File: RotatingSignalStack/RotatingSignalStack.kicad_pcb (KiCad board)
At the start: 2 copper layers, 92 parts, among them IC2 STM32H562RIT6, J2 Conn_01x04, J3 RJ45_LED_Shielded, SW1 SW_Push, SW2 Boot Switch, SW5 SW_Push, SW6 SW_Push, SW7 SW_Push, T1 GMG116S1202R, U1 TMAG5273C1QDBVR, U2 AP63203WU-7, U3 SN65HVD232, U4 DP83825I, U5 SG-210STF 50.0000ML0, U6 USBLC6-2SC6, U7 USBLC6-4SC6

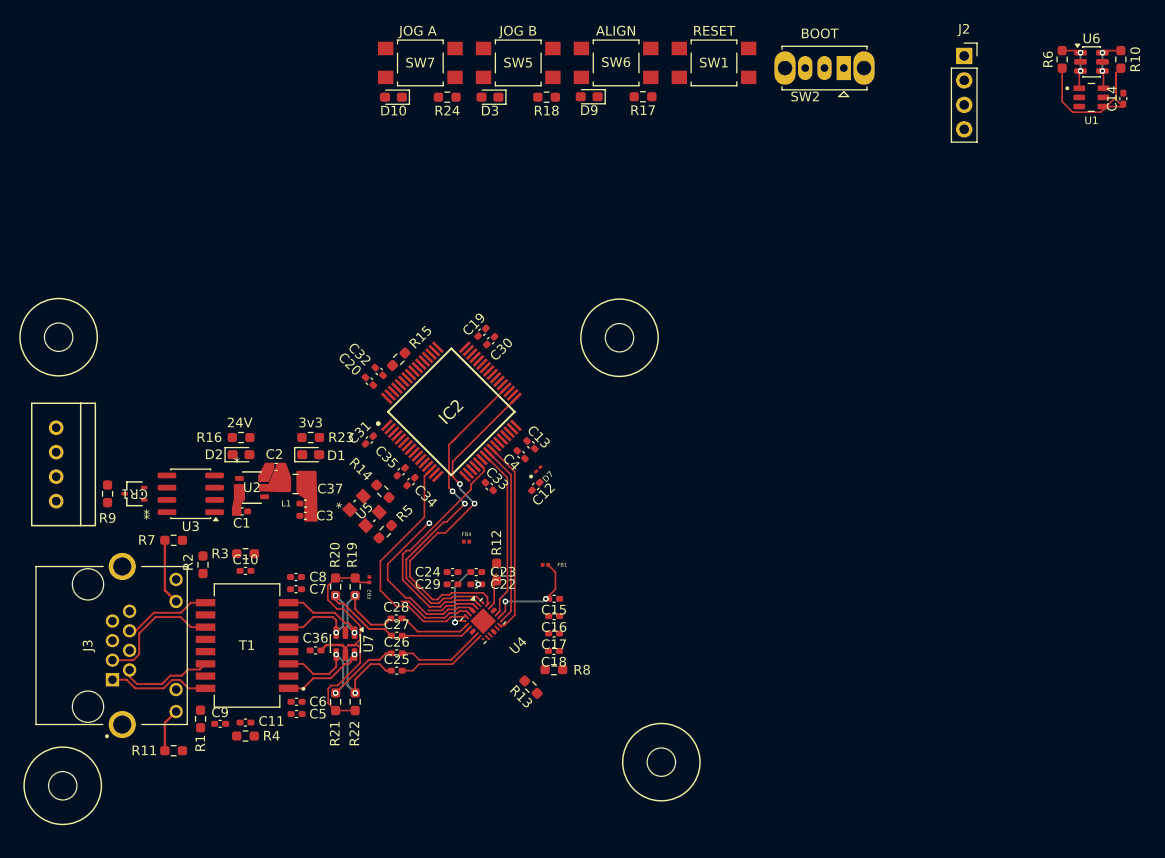
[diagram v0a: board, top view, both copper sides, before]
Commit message: Finished traces, added silkscreen
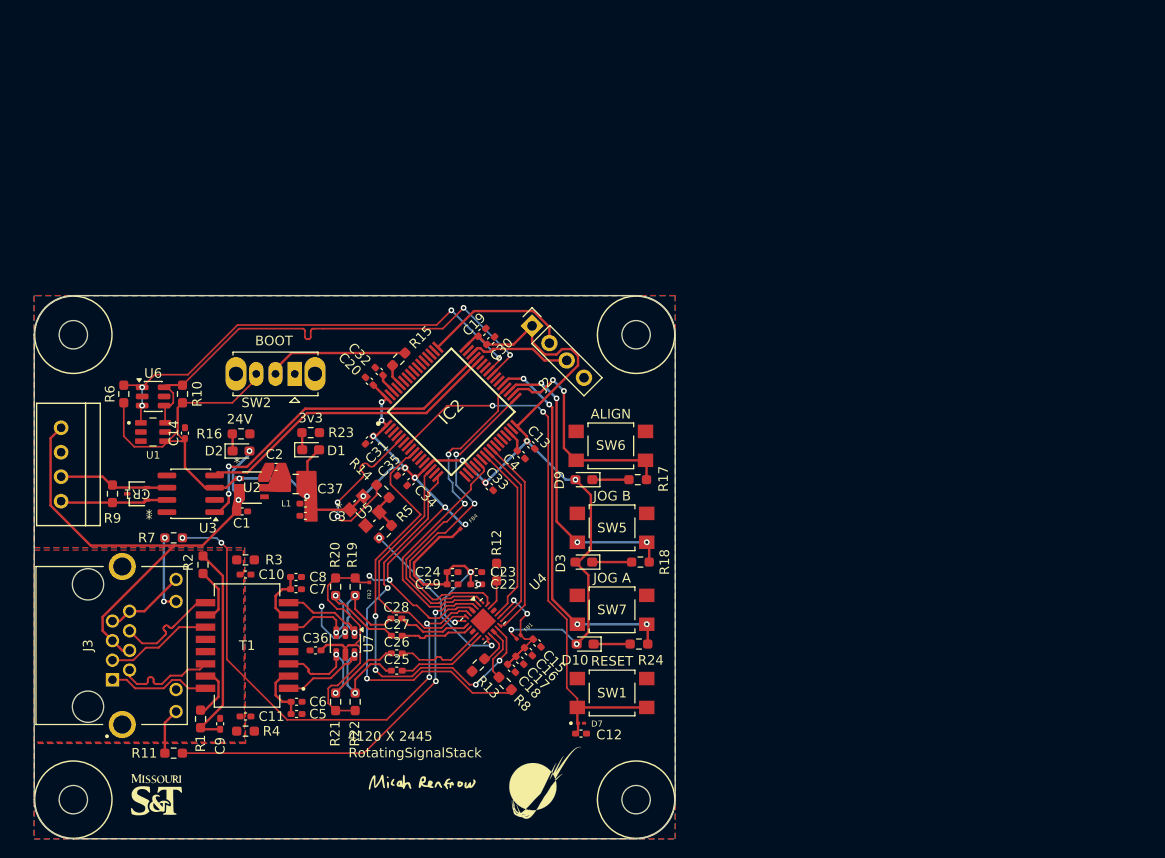
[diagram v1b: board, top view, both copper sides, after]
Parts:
- added G***: LOGO, Silkscreens:MST, F.Cu at (136.9, 107.4)
- added G***: LOGO, LOGO, F.Cu at (164.5, 106.2)
- added G***: LOGO, MRDT_Silkscreens:0_MRDT_Logo_7.5mm, F.Cu at (177.3, 106.2)
- moved C14 103.4 mm to (139.9, 69.9)
- moved R6 103.4 mm to (133.5, 65.8)
- moved U1 103.4 mm to (136.5, 69.8)
- moved R10 103.4 mm to (139.6, 65.8)
- moved U6 103.4 mm to (136.6, 66.1)
- moved SW1 66.3 mm to (184.2, 96.9)
- moved SW2 65.2 mm to (151.3, 63.8)
- moved D10 60.2 mm to (181.4, 91.8)
- moved R24 60.2 mm to (187.0, 91.8)
- moved SW7 60.2 mm to (184.2, 88.2)
- moved J2 52.9 mm to (175.9, 58.8), turned to 45 degrees
- moved D3 49.2 mm to (181.3, 83.3)
- moved R18 49.2 mm to (187.1, 83.3)
- moved SW5 49.2 mm to (184.2, 79.7)
- moved D9 39.8 mm to (181.3, 74.7)
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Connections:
- net Net-(U4-RD+) renamed /PHY/RD+
- net Net-(U4-RD-) renamed /PHY/RD-
- net Net-(U4-TD+) renamed /PHY/TD+
- net Net-(U4-TD-) renamed /PHY/TD-
- IC2 pad 3: /Buttons/JOG B -> unconnected-(IC2-PC14-OSC32_IN-Pad3)
- IC2 pad 34: unconnected-(IC2-PB13-Pad34) -> /Buttons/ALIGN
- IC2 pad 35: unconnected-(IC2-PB14-Pad35) -> /Buttons/JOG B
- IC2 pad 37: unconnected-(IC2-PC6-Pad37) -> /Buttons/JOG A
- IC2 pad 4: /Buttons/JOG A -> unconnected-(IC2-PC15-OSC32_OUT-Pad4)
- IC2 pad 6: /Buttons/ALIGN -> unconnected-(IC2-PH1-OSC_OUT-Pad6)
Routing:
- net VBAT: track 37.7 -> 187.6 mm, vias 1 -> 18
- net Net-(IC2-NRST): track 0.00 -> 58.3 mm, vias 0 -> 2
- net VBUS: track 0.00 -> 53.9 mm, vias 0 -> 2
- net /Compass/I2C3_SDA: track 5.73 -> 52.7 mm
- net /PHY/MDC: track 0.00 -> 46.4 mm, vias 0 -> 4
- net Net-(U4-LED0/S(ANEG_Dis)): track 8.18 -> 52.8 mm, vias 0 -> 4
- net /Compass/I2C3_SCL: track 6.09 -> 50.0 mm, vias 2 -> 4
- net /PHY/MDIO: track 0.00 -> 40.8 mm, vias 0 -> 2
- net /Buttons/JOG A: track 0.00 -> 39.6 mm, vias 0 -> 4
- net /CAN/DCAN1_TX: track 0.00 -> 35.9 mm, vias 0 -> 2
- net Net-(U4-50MHzOut/LED2/S(RX_DV_EN)): track 5.49 -> 41.3 mm, vias 0 -> 2
- net /CAN/DCAN1_RX: track 0.00 -> 32.3 mm
- net /Buttons/JOG B: track 0.00 -> 31.1 mm, vias 0 -> 4
- net /Buttons/ALIGN: track 0.00 -> 23.7 mm, vias 0 -> 2
- net Net-(C9-Pad1): track 0.00 -> 21.7 mm
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- added copper zone on F.Cu, net GNDPWR
- added copper zone on B.Cu, net VSSA
- added copper zone on F.Cu, net VSSA
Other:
- board outline added: 66.5 x 56.4 mm
- board text added: "4120 X 2445"
- board text added: "RotatingSignalStack"

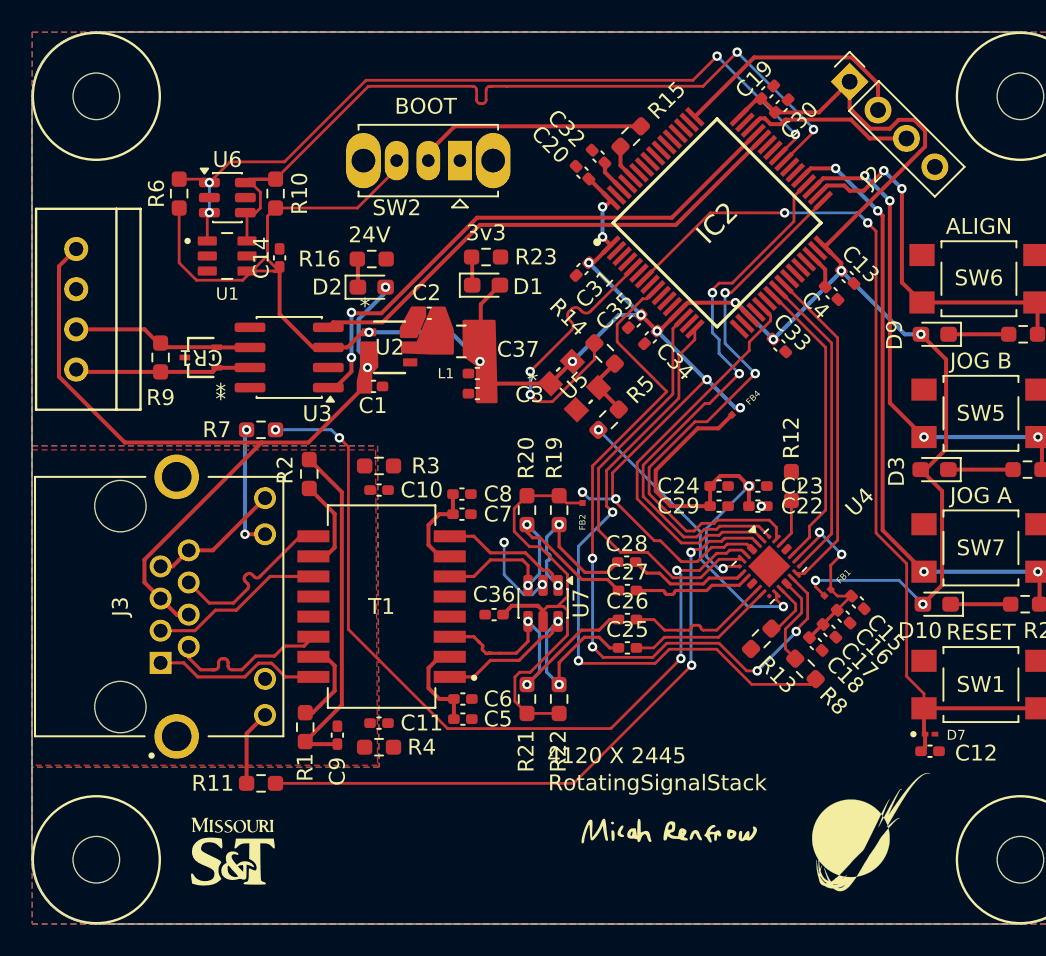
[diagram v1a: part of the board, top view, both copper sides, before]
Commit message: More changes
compass and oki conn and 6 pin conn with the old DIR/EN/STP/COM, fix trace length, under 50 mil Vbus, tree branch
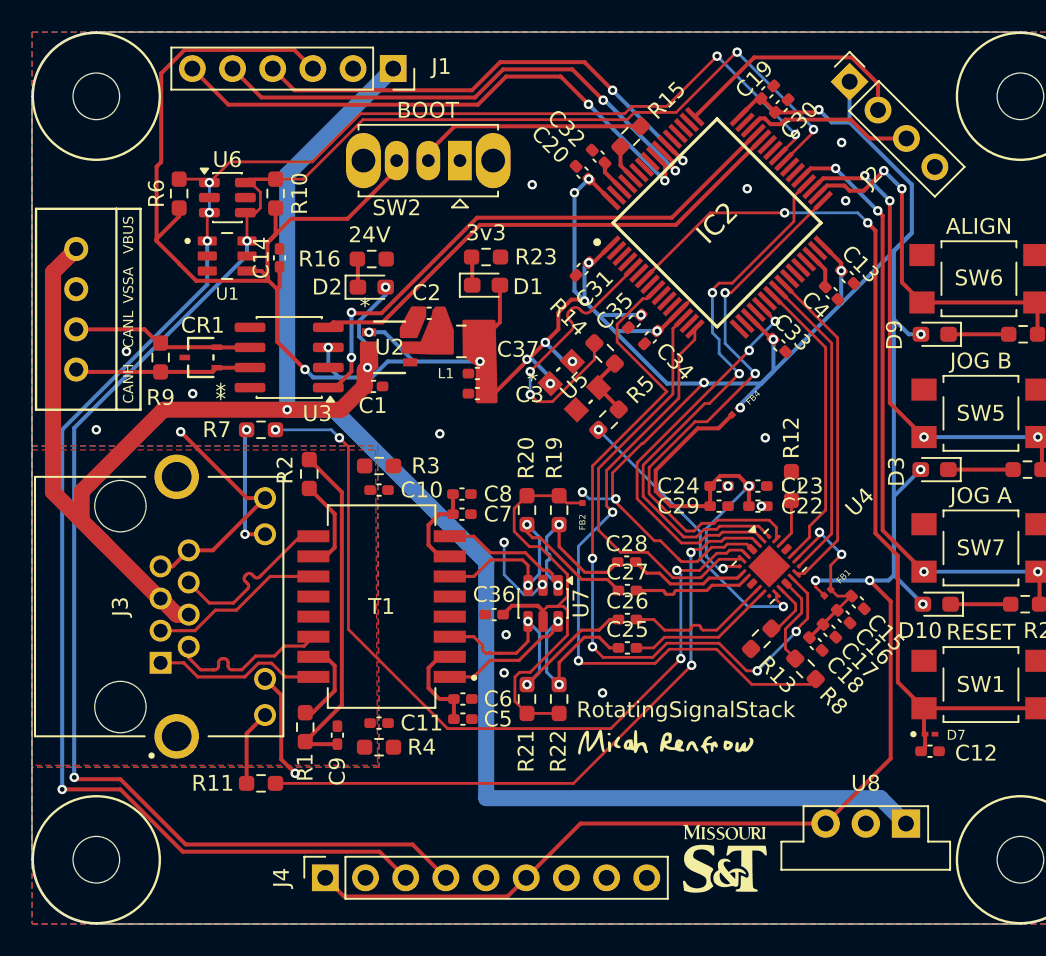
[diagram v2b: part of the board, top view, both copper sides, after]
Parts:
- removed the G*** at (177.3, 106.2)
- added J1: Conn_01x06, Connector_PinSocket_2.54mm:PinSocket_1x06_P2.54mm_Vertical, F.Cu at (147.0, 57.9)
- added J4: Conn_01x09, Connector_PinSocket_2.54mm:PinSocket_1x09_P2.54mm_Vertical, F.Cu at (142.7, 109.1)
- added U8: OKI-78SR-3.3_1.5-W36-C, Converter_DCDC:Converter_DCDC_Murata_OKI-78SR_Vertical, F.Cu at (179.5, 105.7)
- R23: value 1.5k -> 330
- moved G*** 31.1 mm to (168.0, 107.9)
- moved G*** 5.62 mm to (164.2, 100.6)
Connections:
- net /Compass/I2C3_SCL renamed SCL
- net /Compass/I2C3_SDA renamed SDA
- IC2 pad 54: unconnected-(IC2-PD2-Pad54) -> EN
- IC2 pad 55: unconnected-(IC2-PB3-Pad55) -> STP
- IC2 pad 56: unconnected-(IC2-PB4-Pad56) -> DIR
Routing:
- net VBAT: track 187.6 -> 290.4 mm, vias 18 -> 26
- net VBUS: track 53.9 -> 142.8 mm, vias 2 -> 3
- net SDA: track 52.7 -> 115.5 mm, vias 2 -> 4
- net SCL: track 50.0 -> 112.5 mm, vias 4 -> 6
- net DIR: track 0.00 -> 36.1 mm, vias 0 -> 2
- net STP: track 0.00 -> 33.8 mm, vias 0 -> 2
- net EN: track 0.00 -> 31.2 mm, vias 0 -> 2
- net VSSA: track 13.7 -> 27.6 mm, vias 3 -> 18
- net /PHY/TX_EN: track 25.4 -> 26.5 mm, vias 0 -> 2
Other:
- board text added: "CANH"
- board text added: "CANL"
- board text added: "VBUS"
- board text added: "VSSA"
- board text removed: "4120 X 2445"

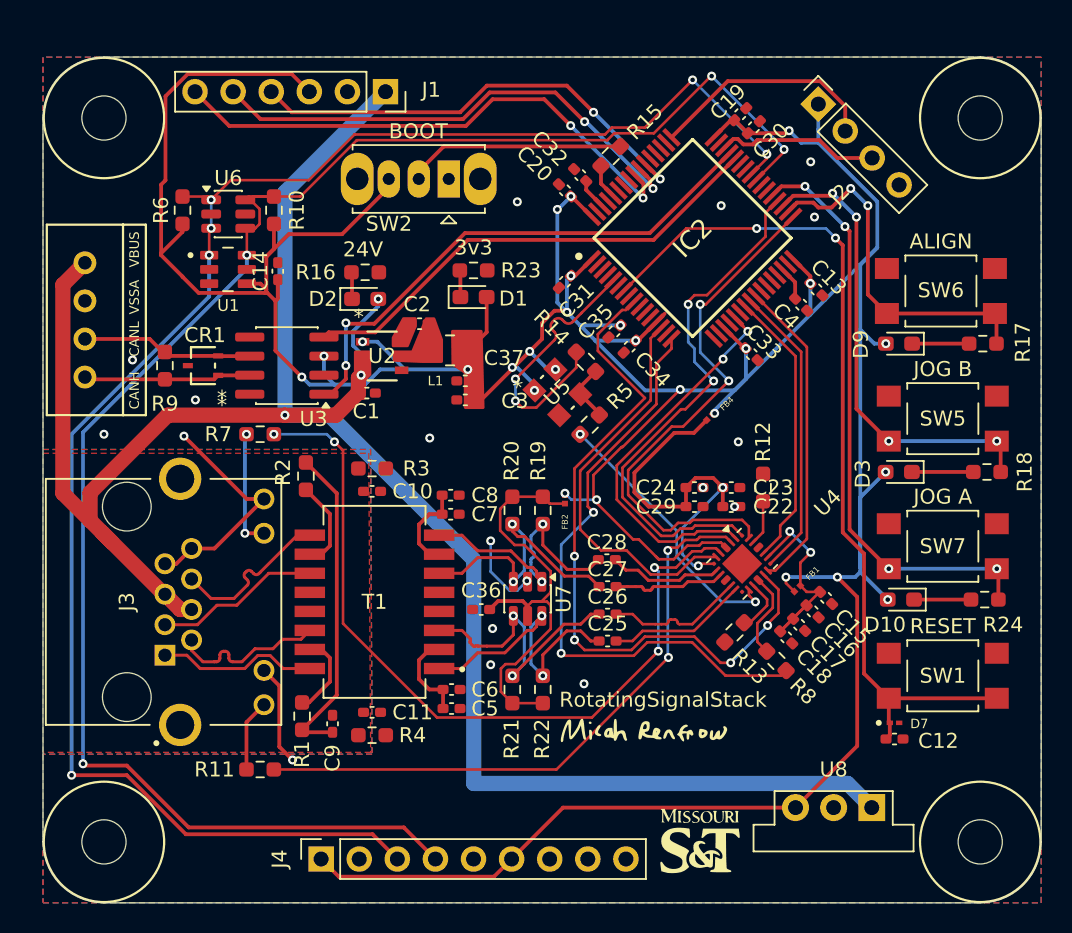
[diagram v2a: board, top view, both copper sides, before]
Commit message: Added ground edges and fixed capacitors and layout issues
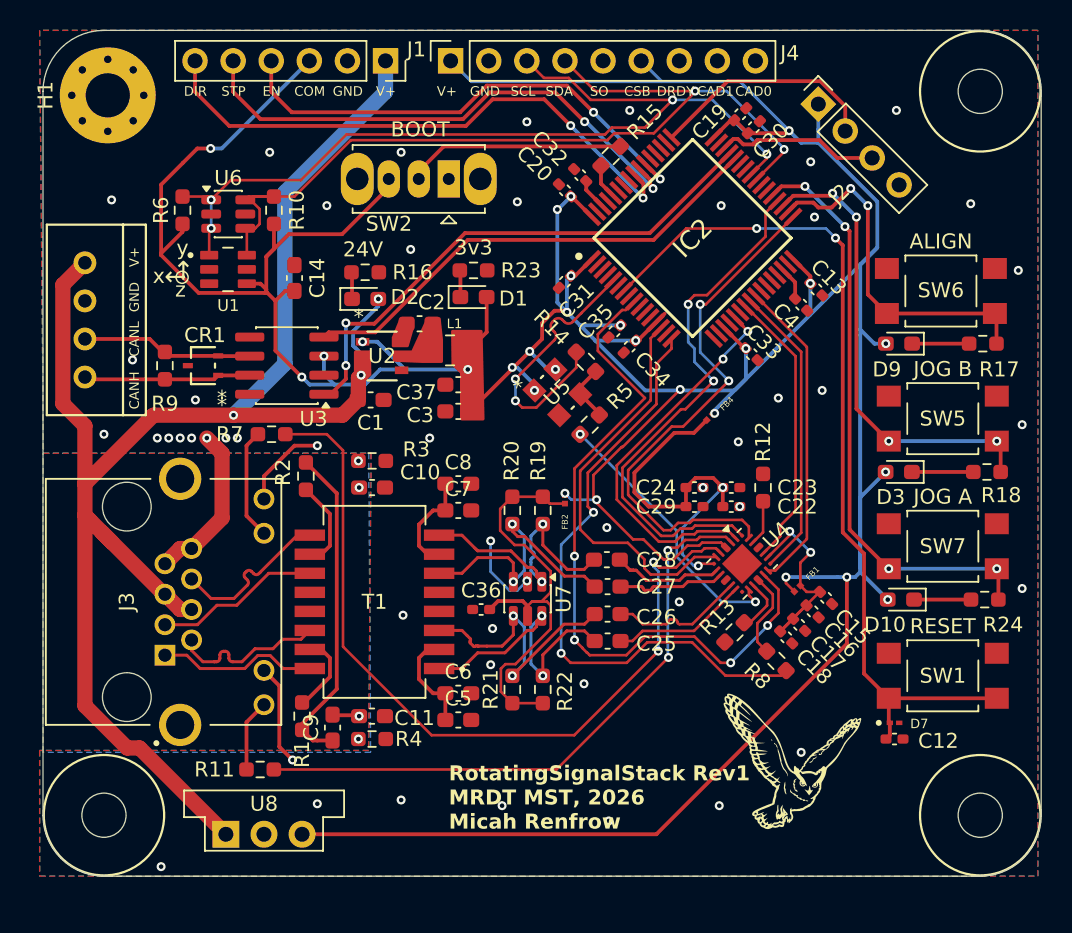
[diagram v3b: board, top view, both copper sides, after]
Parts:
- removed the G*** at (168.0, 107.9)
- C1, C10, C11, C14, C2, C25, C26, C27, C28, C3, C37, C5, C6, C7, C8, C9: footprint Capacitor_SMD:C_0402_1005Metric_Pad0.74x0.62mm_HandSolder -> Capacitor_SMD:C_0603_1608Metric_Pad1.08x0.95mm_HandSolder
- G***: moved to B.Cu
- H1: footprint MRDT_Drill_Holes:4_40_Hole_Corner -> MountingHole:MountingHole_3.2mm_M3_Pad_Via
- moved J4 53.9 mm to (151.4, 55.9)
- moved U8 43.1 mm to (136.4, 107.4), turned to 0 degrees
- moved G*** 19.6 mm to (157.5, 82.2), turned to 180 degrees
- moved H1 6.67 mm to (128.5, 58.2)
- moved J1 2.06 mm to (147.0, 55.9)
- moved H2 1.78 mm to (182.7, 61.9)
- moved H3 1.78 mm to (132.3, 102.2)
- moved H4 1.78 mm to (182.7, 102.2)
- moved C14 1.20 mm to (141.0, 70.4)
- moved C8 0.92 mm to (151.9, 84.1)
- moved C3 0.89 mm to (151.9, 79.2)
- moved C5 0.88 mm to (151.9, 99.8)
- moved R7 0.76 mm to (139.4, 80.8)
- moved C7 0.57 mm to (151.9, 85.9)
- moved C37 0.53 mm to (151.9, 77.5)
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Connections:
- C1 pad 2: VSSA -> GND
- C10 pad 2: VSSA -> GND
- C11 pad 2: VSSA -> GND
- C12 pad 2: VSSA -> GND
- C13 pad 1: VBAT -> +3V3
- C13 pad 2: VSSA -> GND
- C14 pad 1: VBAT -> +3V3
- C14 pad 2: VSSA -> GND
- C15 pad 1: VSSA -> GND
- C16 pad 1: VSSA -> GND
- C17 pad 1: VSSA -> GND
- C18 pad 1: VSSA -> GND
- C19 pad 1: VBAT -> +3V3
- C19 pad 2: VSSA -> GND
- C20 pad 1: VBAT -> +3V3
- C20 pad 2: VSSA -> GND
- C22 pad 2: VSSA -> GND
- C23 pad 2: VSSA -> GND
- C24 pad 2: VSSA -> GND
- C29 pad 2: VSSA -> GND
- C3 pad 1: VBAT -> +3V3
- C3 pad 2: VSSA -> GND
- C30 pad 1: VBAT -> +3V3
- C30 pad 2: VSSA -> GND
- C31 pad 1: VBAT -> +3V3
- C31 pad 2: VSSA -> GND
- C32 pad 1: VSSA -> GND
- C33 pad 1: VBAT -> +3V3
- C33 pad 2: VSSA -> GND
- C34 pad 1: VBAT -> +3V3
- C34 pad 2: VSSA -> GND
- C35 pad 1: VBAT -> +3V3
- C35 pad 2: VSSA -> GND
- C36 pad 2: VSSA -> GND
- C37 pad 1: VBAT -> +3V3
- C37 pad 2: VSSA -> GND
- C4 pad 1: VSSA -> GND
- C5 pad 2: VSSA -> GND
- C6 pad 2: VSSA -> GND
- C7 pad 2: VSSA -> GND
- C8 pad 2: VSSA -> GND
- CR1 pad 3: VSSA -> GND
- Conn1 pad 2: VSSA -> GND
- D1 pad 2: VBAT -> +3V3
- D10 pad 2: +3.3V -> +3V3
- D3 pad 2: +3.3V -> +3V3
- D7 pad 2: VSSA -> GND
- D9 pad 2: +3.3V -> +3V3
- FB1 pad 2: VBAT -> +3V3
- FB2 pad 1: VBAT -> +3V3
- FB4 pad 2: VBAT -> +3V3
- IC2 pad 1: VBAT -> +3V3
- IC2 pad 12: VSSA -> GND
- IC2 pad 13: VBAT -> +3V3
- IC2 pad 18: VSSA -> GND
- IC2 pad 19: VBAT -> +3V3
- IC2 pad 31: VSSA -> GND
- IC2 pad 32: VBAT -> +3V3
- IC2 pad 47: VSSA -> GND
- IC2 pad 48: VBAT -> +3V3
- IC2 pad 63: VSSA -> GND
- IC2 pad 64: VBAT -> +3V3
- J1 pad 2: VSSA -> GND
- J1 pad 3: VBAT -> +3V3
- J2 pad 1: VBAT -> +3V3
- J2 pad 4: VSSA -> GND
- J3 pad 11: VSSA -> GND
- J3 pad 7: VSSA -> GND
- J3 pad 8: VSSA -> GND
- J3 pad 9: VSSA -> GND
- J4 pad 1: VBAT -> +3V3
- J4 pad 2: VSSA -> GND
- J4 pad 6: VBAT -> +3V3
- J4 pad 8: VSSA -> GND
- J4 pad 9: VSSA -> GND
- L1 pad 2: VBAT -> +3V3
- R10 pad 1: VBAT -> +3V3
- R12 pad 1: VSSA -> GND
- R13 pad 1: VSSA -> GND
- R16 pad 1: VSSA -> GND
- R23 pad 1: VSSA -> GND
- R3 pad 2: VSSA -> GND
- R4 pad 2: VSSA -> GND
- R6 pad 1: VBAT -> +3V3
- SW1 pad 2: VSSA -> GND
- SW2 pad 1: VSSA -> GND
- SW2 pad 3: VBAT -> +3V3
- SW5 pad 1: VSSA -> GND
- SW6 pad 1: VSSA -> GND
- SW7 pad 1: VSSA -> GND
- U1 pad 2: VSSA -> GND
- U1 pad 3: VSSA -> GND
- U1 pad 4: VBAT -> +3V3
- U1 pad 5: VSSA -> GND
- U2 pad 1: VBAT -> +3V3
- U2 pad 4: VSSA -> GND
- U3 pad 2: VSSA -> GND
- U3 pad 3: VBAT -> +3V3
- U4 pad 21: VSSA -> GND
- U4 pad 25: VSSA -> GND
- U4 pad 3: VBAT -> +3V3
- U4 pad 9: VSSA -> GND
- U5 pad 1: VBAT -> +3V3
- U5 pad 2: VSSA -> GND
- U5 pad 4: VBAT -> +3V3
- U6 pad 2: VSSA -> GND
- U7 pad 2: VSSA -> GND
- U8 pad 2: VSSA -> GND
- U8 pad 3: VBAT -> +3V3
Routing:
- net +3V3: track 0.00 -> 307.7 mm, vias 0 -> 27
- net VBAT: track 290.4 -> 0.00 mm, vias 26 -> 0
- net SDA: track 115.5 -> 59.7 mm, vias 4 -> 2
- net SCL: track 112.5 -> 59.6 mm, vias 6 -> 4
- net VBUS: track 142.8 -> 111.7 mm
- net GND: track 0.00 -> 28.8 mm, vias 0 -> 49
- net VSSA: track 27.6 -> 0.00 mm, vias 18 -> 0
- net STP: track 33.8 -> 35.9 mm
- net EN: track 31.2 -> 33.3 mm
- net DIR: track 36.1 -> 38.2 mm
- net GNDPWR: track 0.00 -> 1.79 mm, vias 0 -> 4
- net Net-(U4-LED0/S(ANEG_Dis)): track 52.8 -> 54.5 mm, vias 4 -> 2
- net Net-(C7-Pad1): track 6.00 -> 6.92 mm
- net Net-(C5-Pad1): track 6.07 -> 6.92 mm
- net /Ethernet and Magnetics/LED0: track 7.92 -> 7.40 mm, vias 2 -> 0
- added copper zone on B.Cu, net GND
- added copper zone on F.Cu, net GND
- added copper zone on B.Cu, net GNDPWR
- removed copper zone on F.Cu, net GNDPWR
- removed copper zone on B.Cu, net VSSA
- removed copper zone on F.Cu, net VSSA
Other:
- board text added: "CAD0"
- board text added: "CAD1"
- board text added: "COM"
- board text added: "CSB"
- board text added: "DIR"
- board text added: "DRDY"
- board text added: "EN"
- board text added: "GND"
- board text added: "RotatingSignalStack Rev1 MRDT MST, 2026 Micah Renfrow"
- board text added: "SCL"
- board text added: "SDA"
- board text added: "SO"
- board text added: "STP"
- board text added: "V+"
- board text added: "x"
- board text added: "y"
- board text added: "z"
- board text added: "←"
- board text removed: "RotatingSignalStack"
- board text removed: "VBUS"
- board text removed: "VSSA"
